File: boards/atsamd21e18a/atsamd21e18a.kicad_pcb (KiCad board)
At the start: 4 copper layers, 17.8 x 38.1 mm, 27 parts, among them J1 USB_B_Micro, J2 A, J3 B, J4 SWD_1.27, SW1 RESET, U1 AP7361C_SOT-89-5, U2 ATSAMD21E, Y1 ABS07-32.768KHZ

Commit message: Removed 0.1" SWD pins. Reworked pinout.
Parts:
- renumbered PA14 to JP1, PA15 to JP2
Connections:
- J3 pad 1: +3V3 -> +5V
- J3 pad 10: /PA17 -> /PA15_NO
- J3 pad 11: /PA16 -> /PA14_NO
- J3 pad 12: /PA15_NO -> /~RESET
- J3 pad 13: /PA14_NO -> GND
- J3 pad 2: /~RESET -> +3V3
- J3 pad 3: /SWD_IO -> /PA28
- J3 pad 4: /SWD_CLK -> /PA27
- J3 pad 5: /PA28 -> /PA22
- J3 pad 6: /PA27 -> /PA19
- J3 pad 7: /PA22 -> /PA18
- J3 pad 8: /PA19 -> /PA17
- J3 pad 9: /PA18 -> /PA16
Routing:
- net /~RESET: track 54.0 -> 30.7 mm
- net /SWD_IO: track 27.1 -> 19.1 mm
- net /SWD_CLK: track 23.8 -> 17.1 mm
- net +5V: track 26.6 -> 32.2 mm
- net /PA28: track 5.83 -> 10.7 mm
- net /PA27: track 4.23 -> 8.67 mm
- net /PA22: track 5.69 -> 10.0 mm, vias 0 -> 1
- net /PA15_NO: track 13.2 -> 9.62 mm
- net /PA14_NO: track 15.1 -> 11.6 mm
- net /PA19: track 5.06 -> 8.47 mm
- net /PA16: track 9.99 -> 6.73 mm
- net /PA17: track 8.84 -> 5.82 mm
- net GND: track 23.3 -> 24.9 mm, vias 17 -> 19
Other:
- board text added: "+5V"
- board text removed: "CLK"
- board text removed: "IO"
- board text removed: "SWD"
- board text removed: "VIN"

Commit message: Added consealed 0.1mm header for SWD IO and CLK.
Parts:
- added J5: SWD_2.54, Connector_PinHeader_2.54mm:PinHeader_1x02_P2.54mm_Vertical, B.Cu at (36.8, 52.6)
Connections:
- J3 pad 12: /~RESET -> +3V3
- J3 pad 13: GND -> /~RESET
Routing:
- net /SWD_CLK: track 17.1 -> 20.7 mm
- net /SWD_IO: track 19.1 -> 21.7 mm
- net GND: track 24.9 -> 23.0 mm, vias 19 -> 18
- net +3V3: track 20.3 -> 21.3 mm, vias 10 -> 11
- net /~RESET: track 30.7 -> 31.3 mm
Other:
- board text added: "CLK"
- board text added: "IO"

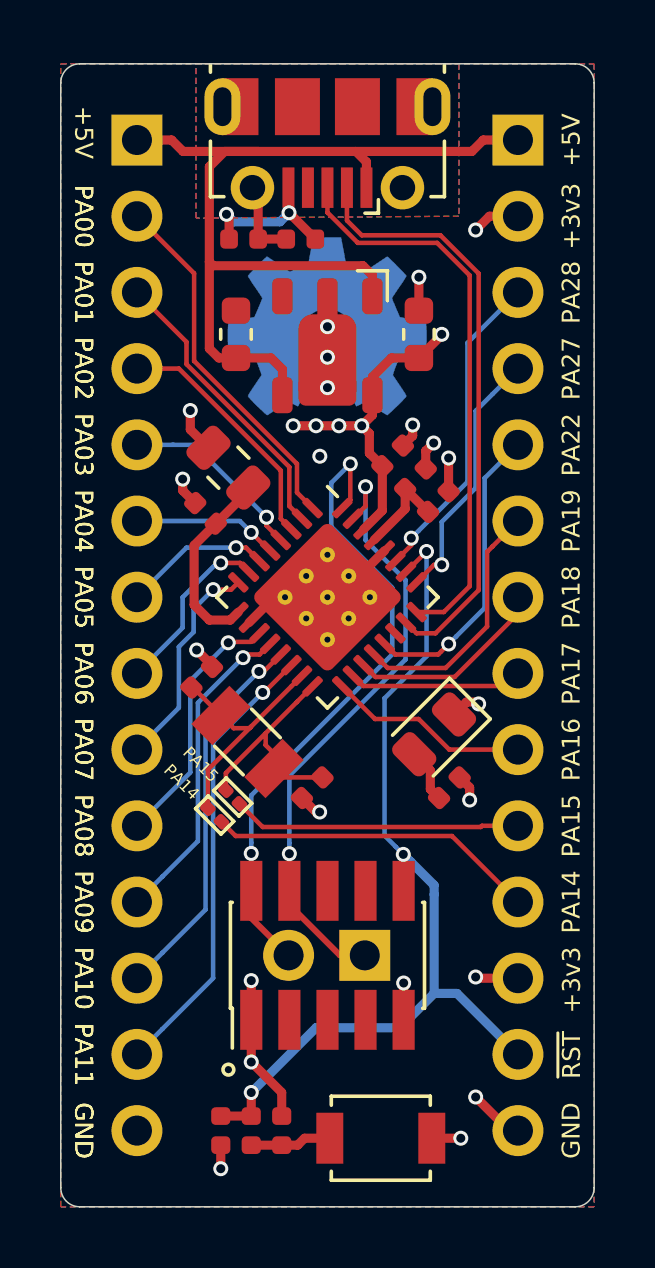
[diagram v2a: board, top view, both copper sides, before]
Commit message: Removed PA14, PA15. If needed, remove X1 and bodge to pads.
Shortened board by 2 rows.

Added castillated edges.

Added 0.1" SWD header.

Put 0.05" SWD header on bottom of board.

Addresses issue #11.
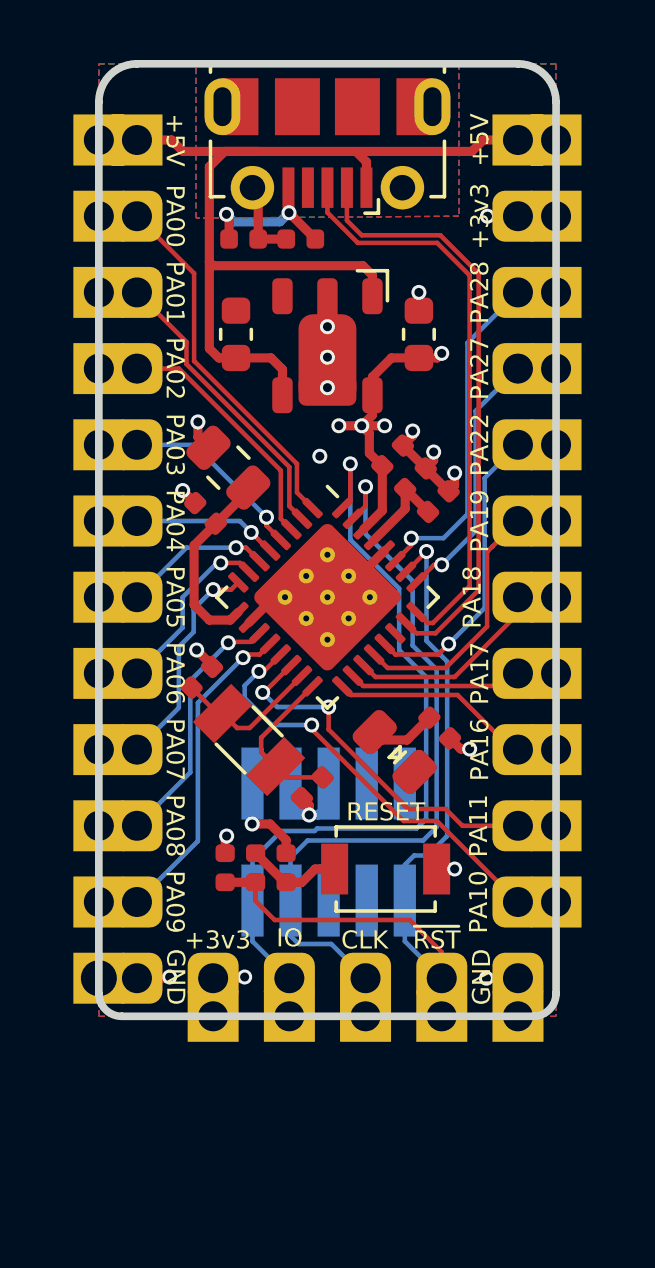
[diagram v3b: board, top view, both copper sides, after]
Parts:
- removed JP1: J_PA14, jkiv-library:J_NO_0201_0603Metric
- removed JP2: J_PA15, jkiv-library:J_NO_0201_0603Metric
- removed REF**: OSHW-Symbol_6.7x6mm_Copper, Symbol:OSHW-Symbol_6.7x6mm_Copper
- J2, J3: footprint Connector_PinHeader_2.54mm:PinHeader_1x14_P2.54mm_Vertical -> Connector_PinHeader_2.54mm:PinHeader_1x12_P2.54mm_Vertical
- J4: moved to B.Cu
- J5: footprint Connector_PinHeader_2.54mm:PinHeader_1x02_P2.54mm_Vertical -> Connector_PinHeader_2.54mm:PinHeader_1x04_P2.54mm_Vertical; moved to F.Cu
- R2, R3: value 4k7 -> 1k
- moved SW1 8.98 mm to (37.5, 49.7)
- moved C9 8.76 mm to (32.1, 49.7), turned to 90 degrees
- moved R2 8.76 mm to (33.2, 49.7), turned to 270 degrees
- moved R3 8.76 mm to (34.2, 49.7)
- moved J5 5.11 mm to (31.8, 53.3)
- moved J4 3.78 mm to (35.6, 48.8), turned to 270 degrees
- moved R1 2.02 mm to (39.3, 45.0), turned to 135 degrees
- moved D1 1.44 mm to (37.8, 45.8), turned to 135 degrees
- moved Y1 0.09 mm to (33.0, 45.4)
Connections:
- J2 pad 12: /PA10 -> GND
- J3 pad 10: /PA15_NO -> /PA11
- J3 pad 11: /PA14_NO -> /PA10
- J3 pad 12: +3V3 -> GND
- J5 pad 1: /SWD_CLK -> +3V3
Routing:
- net /PA14_NO: track 11.6 -> 0.00 mm
- net /PA15_NO: track 9.62 -> 0.00 mm
- net /SWD_CLK: track 20.7 -> 25.4 mm, vias 2 -> 1
- net /SWD_IO: track 21.7 -> 26.2 mm, vias 2 -> 1
- net /~RESET: track 31.3 -> 27.1 mm, vias 3 -> 1
- net /PA14: track 8.29 -> 4.97 mm
- net GND: track 23.0 -> 25.9 mm, vias 18 -> 17
- net /PA10: track 12.9 -> 15.7 mm, vias 1 -> 2
- net +3V3: track 21.3 -> 18.8 mm, vias 11 -> 9
- net /PA11: track 15.1 -> 13.1 mm, vias 1 -> 2
- net +5V: track 32.2 -> 34.1 mm
- net /PA15: track 7.21 -> 5.30 mm
- net /PA28: track 10.7 -> 12.2 mm
- net /PA27: track 8.67 -> 9.64 mm
- net /PA22: track 10.0 -> 11.0 mm
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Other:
- board size 17.8 x 38.1 mm -> 15.2 x 31.8 mm
- board text added: "RESET"
- board text added: "SWD"
- board text removed: "PA14"
- board text removed: "PA15"

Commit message: Incremented version to 2021-01.
Fixed 1.2mm castellation.
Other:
- board text added: "atsamd21e18a 2021-01 fourside.io"
- board text removed: "atsamd21e18a 2020-04 fourside.io"
